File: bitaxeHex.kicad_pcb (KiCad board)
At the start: 4 copper layers, 84.5 x 129.5 mm, 393 parts, among them J1 Screw Terminal, J2 Conn_01x01, J3 Conn_02x05_Odd_Even, J4 ST7789 176x320, J5 Conn_01x04, J6 TC2030-IDC, J7 USB_C_Receptacle_USB2.0, J8 Conn_01x04, J9 Conn_01x04, Q1 2N7002K, SW1 EVQ-9P701P, SW2 EVQ-9P701P, U1 LMR54410, U10 AP7331, U11 AP7331, U12 BM1366_mode1, U13 BM1366_mode1, U14 25MHz, U15 TLV3544, U16 AP7331, U17 AP7331, U18 BM1366_mode0, U19 25MHz, U2 RT9080-33GJ5, U20 BM1366_mode0, U21 TLV3544, U22 BM1366_mode1, U23 AP7331, U24 AP7331, U25 BM1366_mode1, U26 25MHz, U3 TPS546D24ARVFR, U4 MIC5504, U5 SN74AVC4T774, U6 ESP32-S3-WROOM-1, U7 TMP1075, U8 TMP1075, U9 EMC2302, Y1 32.768kHz

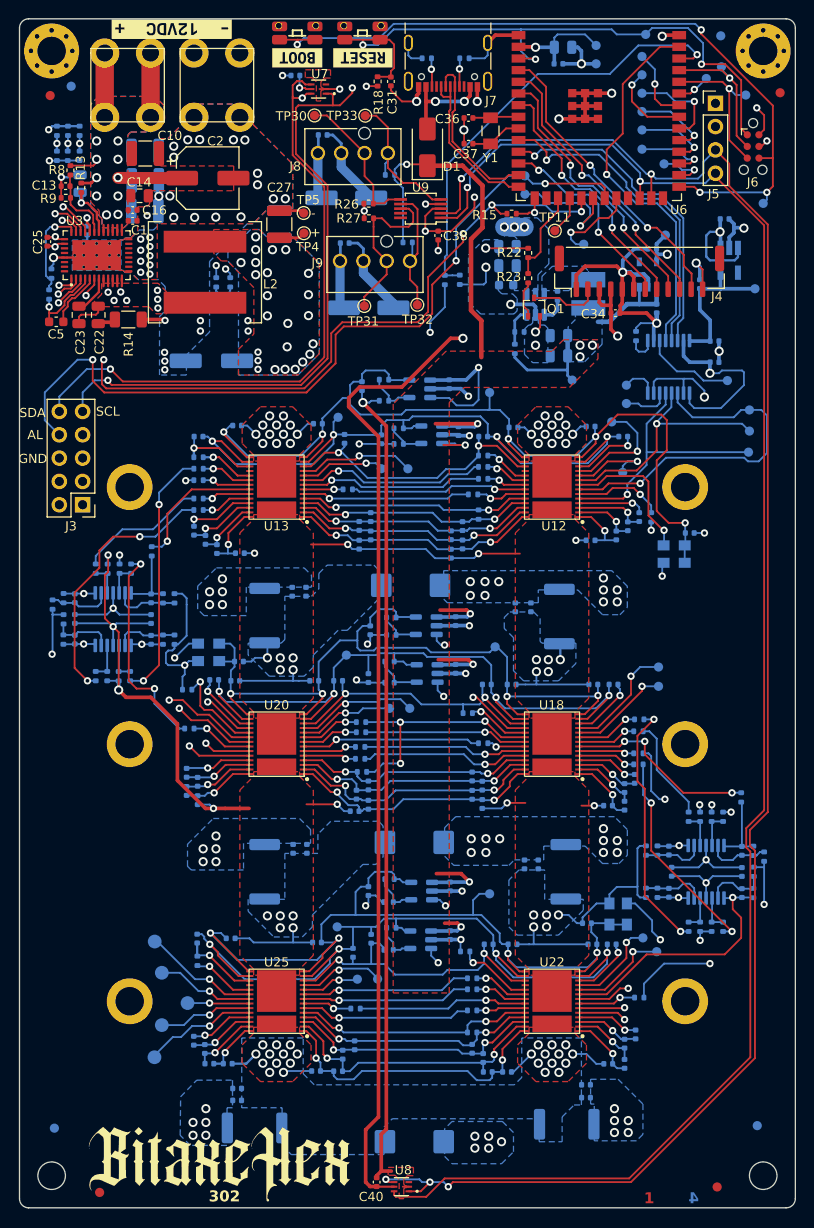
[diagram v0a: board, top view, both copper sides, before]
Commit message: increase size of copper planes, generate final BOM
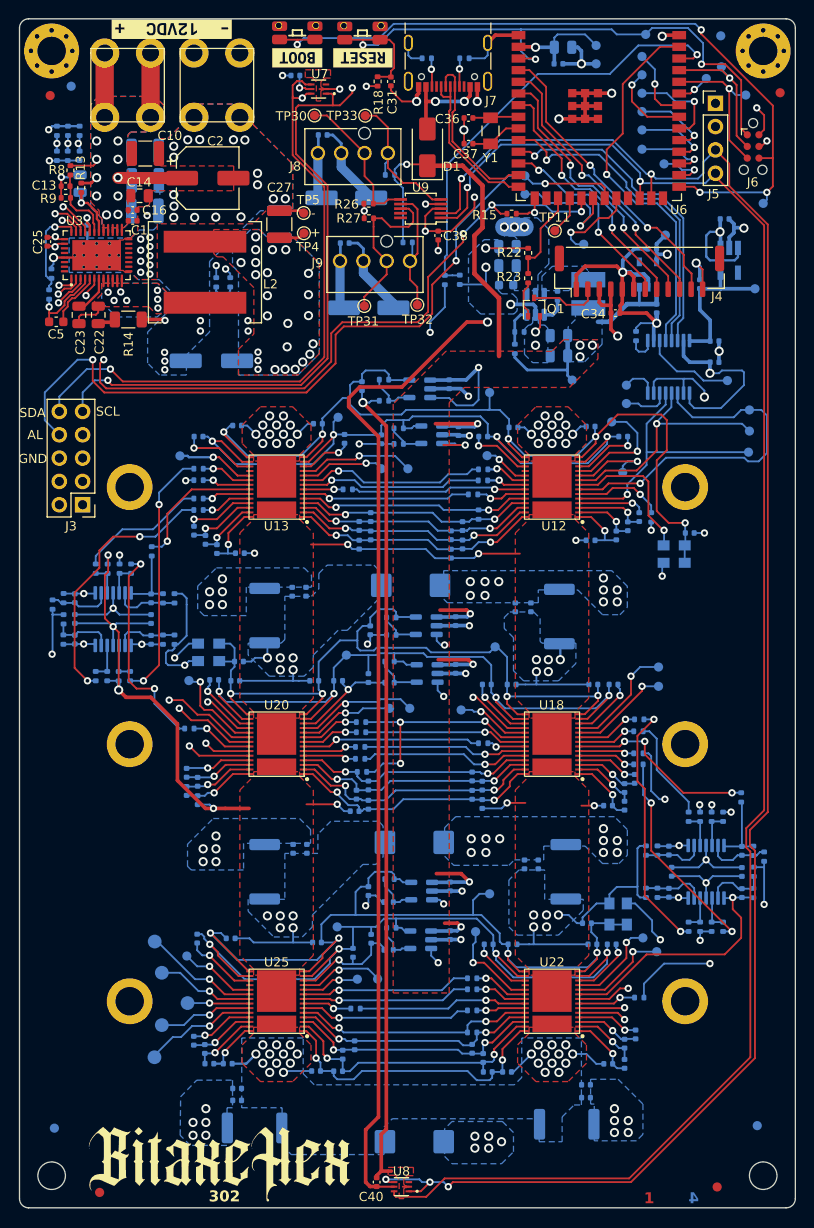
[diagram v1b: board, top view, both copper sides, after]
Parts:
- removed R113: 33, Resistor_SMD:R_0402_1005Metric
- removed the R37 at (100.5, 93.6)
- removed the R45 at (69.5, 93.8)
- removed the R64 at (98.8, 121.6)
- removed the R82 at (68.3, 119.1)
- removed the R99 at (98.5, 147.6)
- added TP38: TestPoint, TestPoint:TestPoint_Pad_D1.0mm, B.Cu at (100.9, 93.6)
- added TP41: TestPoint, TestPoint:TestPoint_Pad_D1.0mm, B.Cu at (67.5, 93.6)
- added TP46: TestPoint, TestPoint:TestPoint_Pad_D1.0mm, B.Cu at (98.1, 121.3)
- added TP49: TestPoint, TestPoint:TestPoint_Pad_D1.0mm, B.Cu at (68.5, 118.1)
- added TP54: TestPoint, TestPoint:TestPoint_Pad_D1.0mm, B.Cu at (99.7, 145.4)
- added TP57: TestPoint, TestPoint:TestPoint_Pad_D1.0mm, B.Cu at (68.2, 148.1)
- J4: value ST7789 176x320 -> Connector-12x1
- SW1, SW2: value EVQ-9P701P -> SWITCH-SPST
- moved R36 0.28 mm to (100.5, 95.1)
- moved R37 0.18 mm to (100.5, 96.3)
- moved C18 0.10 mm to (57.4, 69.0)
- renumbered R105 to R100, R106 to R101, R107 to R102, R108 to R103, R109 to R104, R110 to R105, R111 to R106, R112 to R107, R114 to R108, R38 to R37, R39 to R38, R40 to R39, R41 to R40, R42 to R41, R43 to R42, R44 to R43, R46 to R44, R47 to R45, R48 to R46, R49 to R47, R50 to R48, R51 to R49, R52 to R50, R53 to R51, R54 to R52, R55 to R53, R56 to R54, R57 to R55, R58 to R56, R59 to R57, R60 to R58, R61 to R59, R62 to R60, R63 to R61, R65 to R62, R66 to R63, R67 to R64, R68 to R65, R69 to R66, R70 to R67, R71 to R68, R72 to R69, R73 to R70, R74 to R71, R75 to R72, R76 to R73, R77 to R74, R78 to R75, R79 to R76, R80 to R77, R81 to R78, R83 to R79, R84 to R80, R85 to R81, R86 to R82, R87 to R83, R88 to R84, R89 to R85, R90 to R86, R91 to R87, R92 to R88, R93 to R89, R94 to R90, R95 to R91, R96 to R92, R97 to R93, R98 to R94, R100 to R95, R101 to R96, R102 to R97, R103 to R98, R104 to R99, TP38 to TP39, TP39 to TP40, TP40 to TP42, TP41 to TP43, TP42 to TP44, TP43 to TP45, TP44 to TP47, TP45 to TP48, TP46 to TP50, TP47 to TP51, TP48 to TP52, TP49 to TP53, TP50 to TP55, TP51 to TP56, TP52 to TP58, TP53 to TP59, TP54 to TP60, TP55 to TP61, TP56 to TP62
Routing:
- net GND: track 365.2 -> 345.9 mm
- net /BM1366-1/VDD1: track 195.8 -> 177.5 mm, vias 47 -> 46
- net /BM1366-2/VDD2: track 214.1 -> 197.5 mm
- net Net-(U13-INV_CLKO): track 5.90 -> 8.50 mm
- net Net-(U22-INV_CLKO): track 8.27 -> 10.4 mm
- net /3V3: track 210.6 -> 208.7 mm
- net Net-(U25-INV_CLKO): track 6.80 -> 8.38 mm
- net Net-(U18-INV_CLKO): track 6.77 -> 8.01 mm
- added copper zone on B.Cu, net /Power/SW
- added copper zone on In1.Cu, net /VIN
- added copper zone on In1.Cu, net GND

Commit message: final polishing before gerbers
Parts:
- H3, H4: footprint MountingHole:MountingHole_3mm -> MountingHole:MountingHole_3mm_Pad_Via
- J3: moved to B.Cu
- moved J3 2.43 mm to (54.5, 99.0), turned to 0 degrees
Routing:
- net /BM1366-2/VDD2: track 197.5 -> 191.6 mm
- net /SMB_ALRT: track 98.4 -> 102.1 mm
- net /SCL: track 294.8 -> 297.2 mm
- net /SDA: track 292.3 -> 291.5 mm
- net /BM1366-1/VDD1: track 177.5 -> 176.9 mm

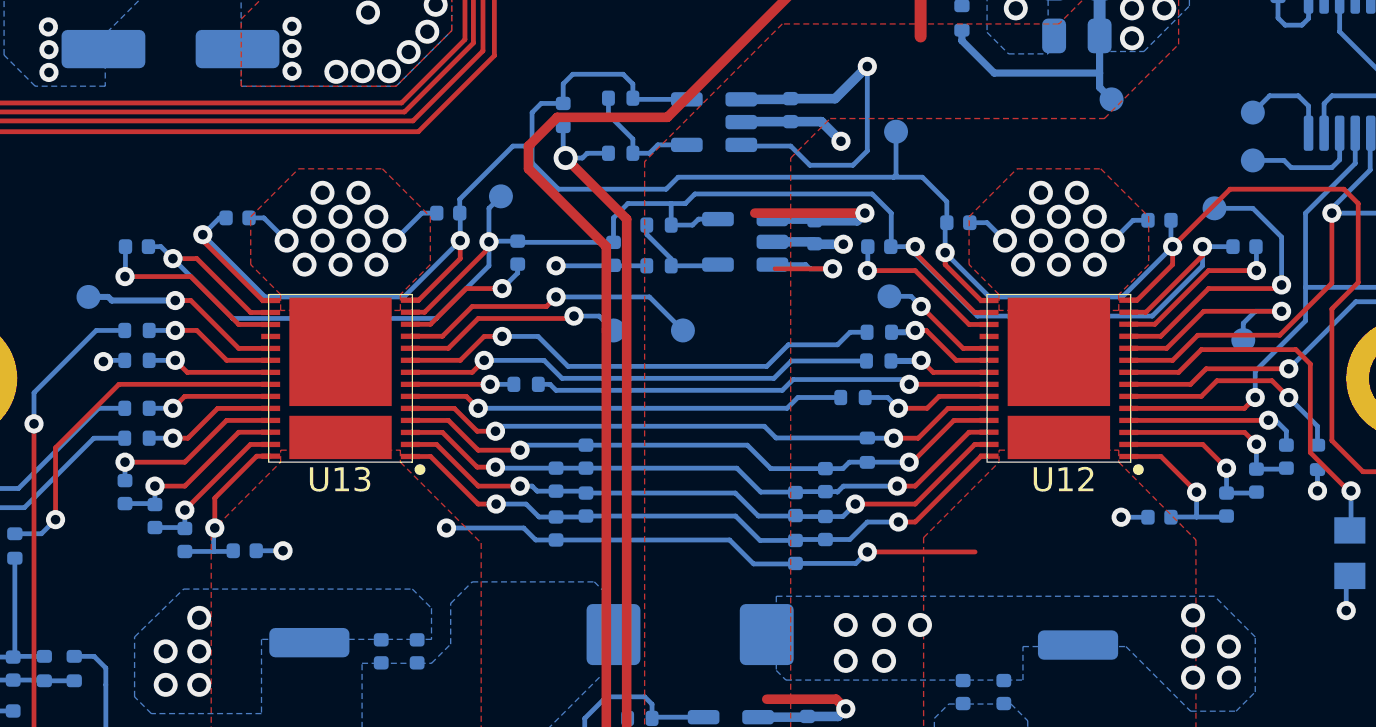
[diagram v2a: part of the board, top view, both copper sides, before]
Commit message: via organizing on In1. removed islands from In1 and In2
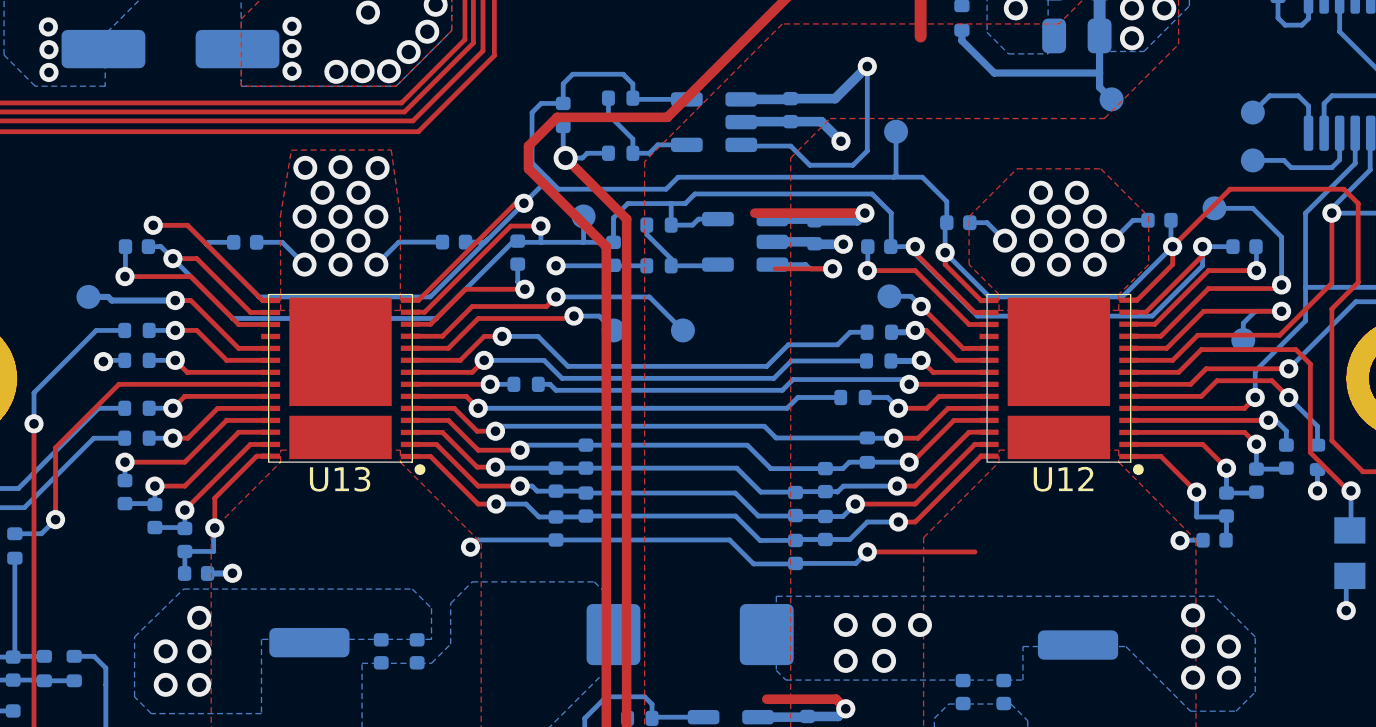
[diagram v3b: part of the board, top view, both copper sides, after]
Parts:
- moved TP36 3.55 mm to (88.2, 90.2)
- moved C52 2.49 mm to (114.5, 103.8)
- moved C72 2.24 mm to (72.0, 105.2)
- moved C70 1.23 mm to (82.7, 91.3)
- moved C74 1.07 mm to (74.0, 91.3)
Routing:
- net /BM1366-1/1V8: track 106.2 -> 113.3 mm
- net GND: track 345.8 -> 347.9 mm, vias 111 -> 112
- net /BM1366-1/0V8: track 78.3 -> 79.6 mm
- net /BM1366-1/VDD1: track 176.9 -> 175.6 mm

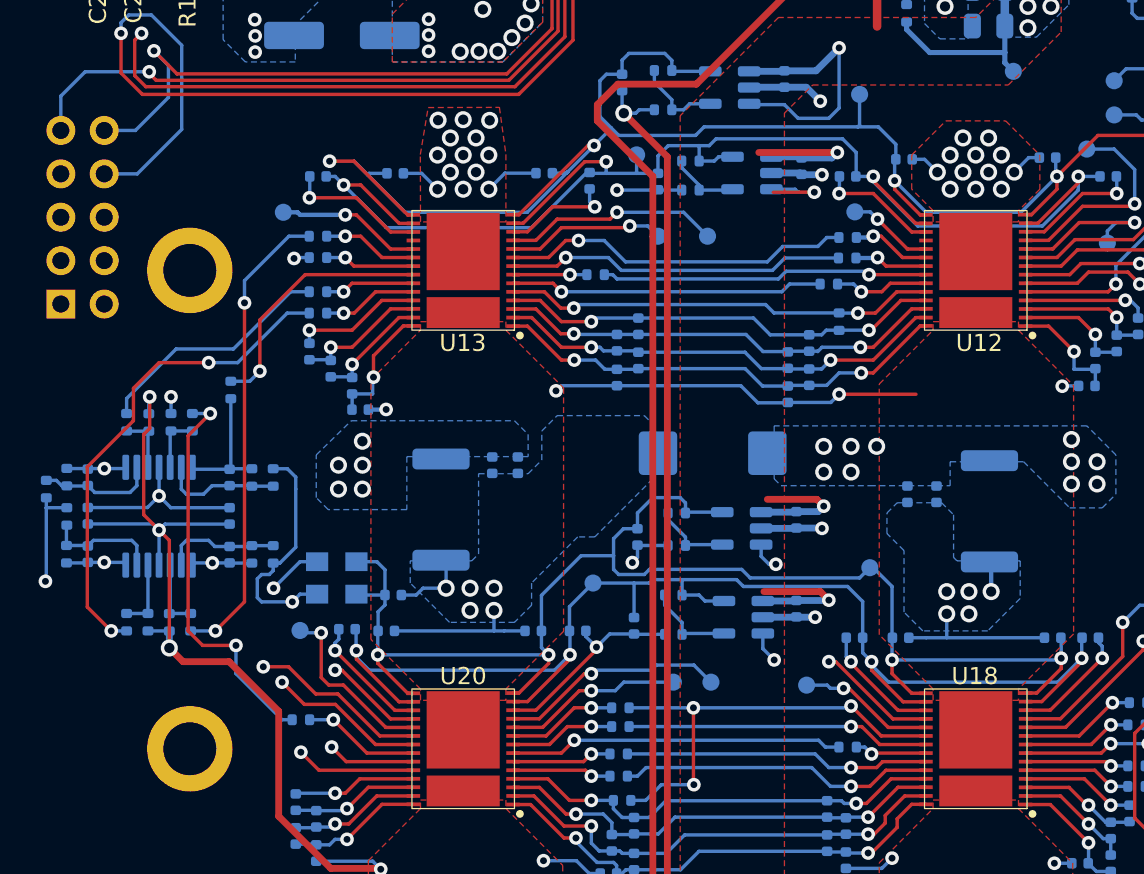
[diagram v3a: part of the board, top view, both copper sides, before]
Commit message: eliminate more traces on In1, expand copper pour a little more
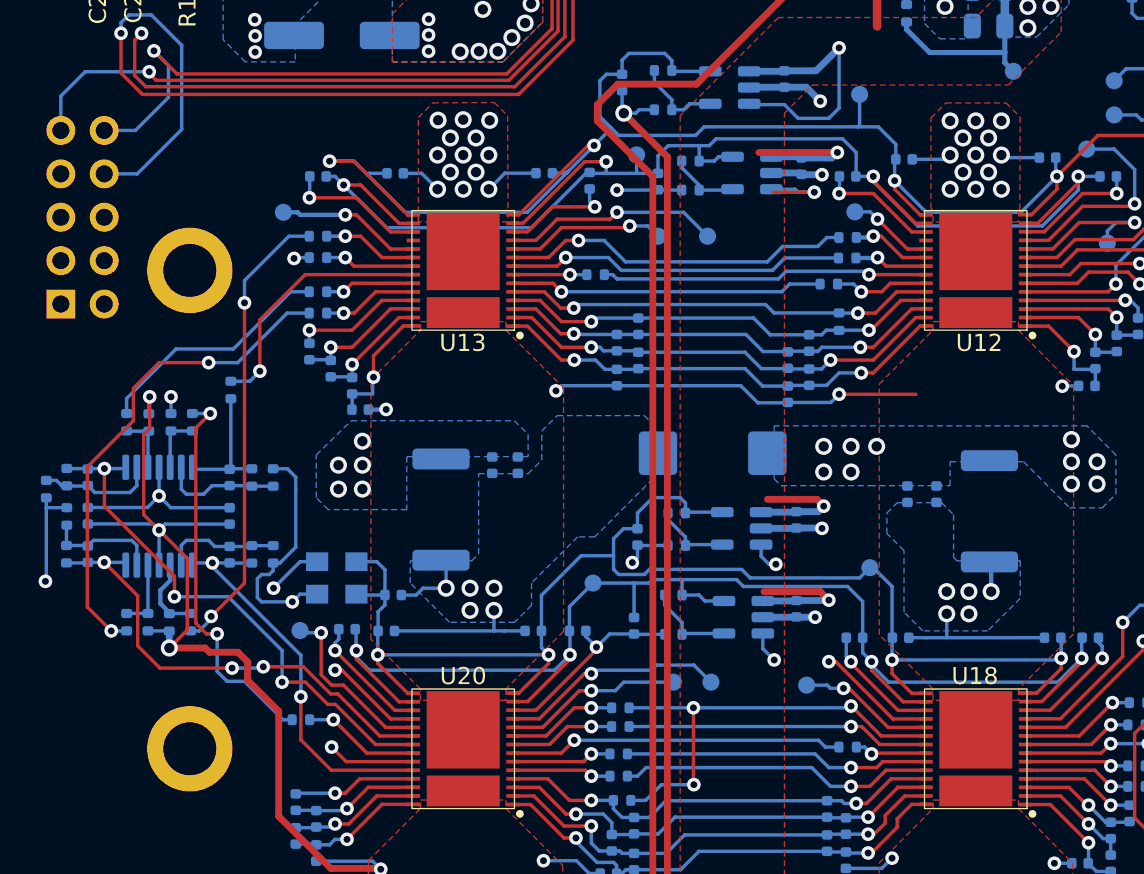
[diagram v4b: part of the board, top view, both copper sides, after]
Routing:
- net /BM1366-2/VDD2: track 191.6 -> 193.1 mm
- net /BM1366-2/NRSTI2: track 26.4 -> 27.7 mm, vias 2 -> 3
- net GND: track 347.9 -> 348.9 mm, vias 112 -> 113
- net /BM1366-2/RO2: track 23.5 -> 22.9 mm
- net /BM1366-1/CO: track 27.5 -> 27.0 mm
- net Net-(U15A-+): track 4.10 -> 4.62 mm
- net /BM1366-2/BI2: track 31.5 -> 31.4 mm, vias 2 -> 3
